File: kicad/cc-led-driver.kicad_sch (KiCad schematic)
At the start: 10 parts, among them Q3 PUMD9, U1 LMR33640ADDAR, U2 LM4040-2.5

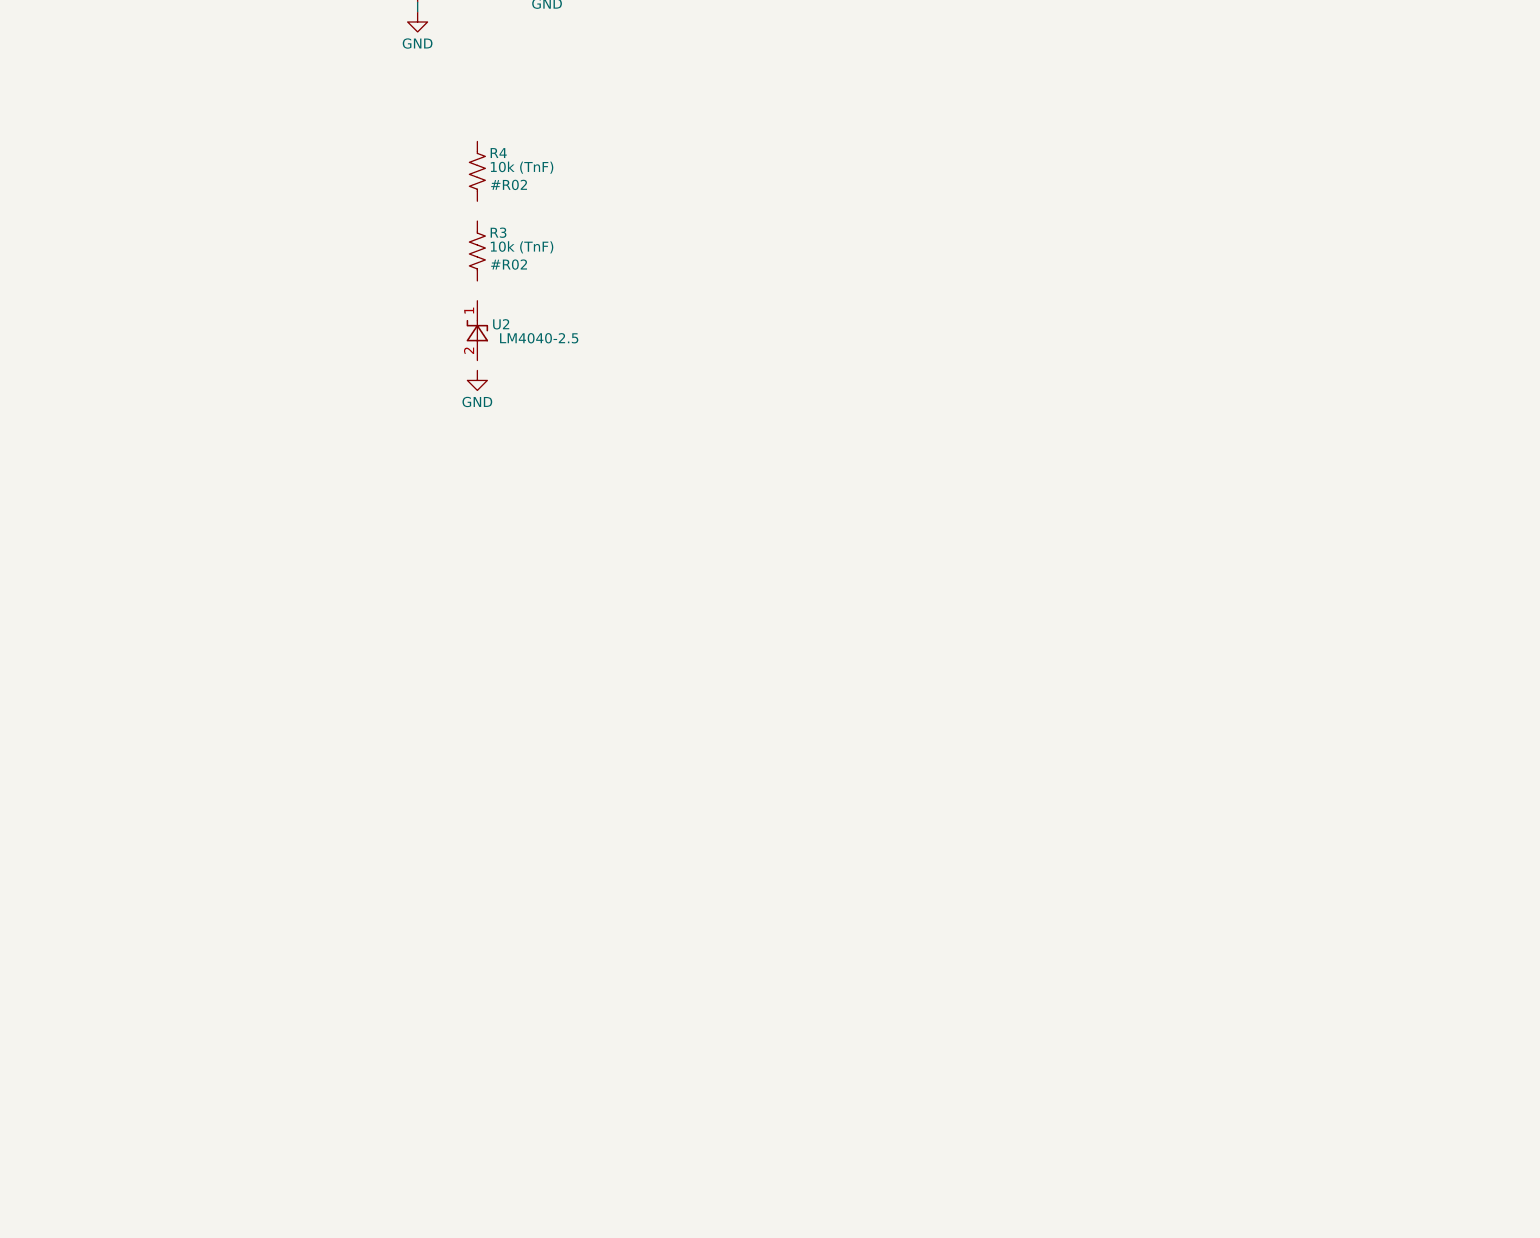
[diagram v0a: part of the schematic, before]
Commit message: gamma correction simulated
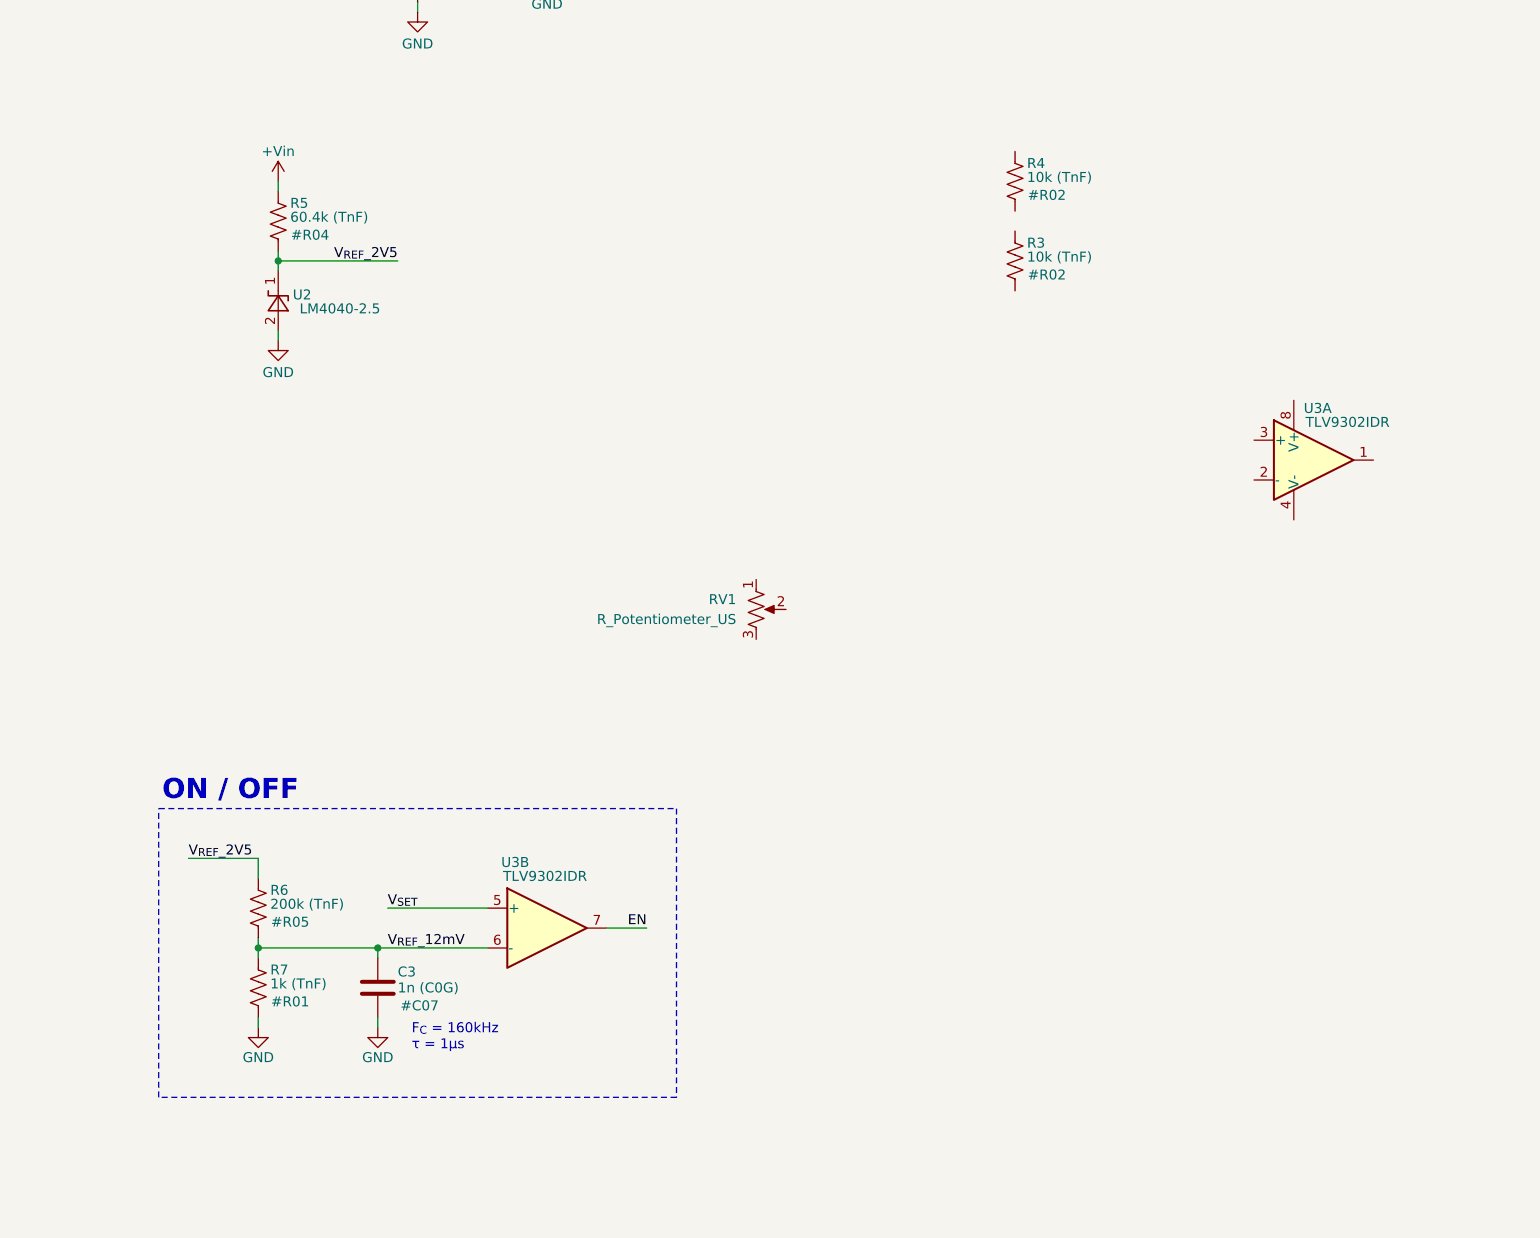
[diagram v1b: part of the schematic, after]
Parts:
- added C3: 1n (C0G), Capacitor_SMD:C_0603_1608Metric, symbol Device:C
- added R5: 60.4k (TnF), Resistor_SMD:R_0603_1608Metric, symbol Device:R_US
- added R6: 200k (TnF), Resistor_SMD:R_0603_1608Metric, symbol Device:R_US
- added R7: 1k (TnF), Resistor_SMD:R_0603_1608Metric, symbol Device:R_US
- added RV1: R_Potentiometer_US, symbol Device:R_Potentiometer_US
- added U3: TLV9302IDR, Package_SO:SOIC-8_3.9x4.9mm_P1.27mm, symbol Amplifier_Operational:TLV9302xD
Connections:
- net GND: now also U2.2 (A), C3.2, R7.2
- net V_{REF}_2V5: now reaches U2.1 (K)
- net V_{REF}_2V5: now also R5.2, R6.1
- new net +Vin: R5.1
- new net EN: U3.7
- new net V_{REF}_12mV: C3.1, R6.2, R7.1, U3.6 (-)
- new net V_{SET}: U3.5 (+)
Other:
- note added: "F_{C} = 160kHz τ = 1μs"
- note added: "ON / OFF"
- moved on the sheet: R3, R4, U2

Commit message: progress on schematic
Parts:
- added C10: DNP, Capacitor_SMD:C_0603_1608Metric, symbol Device:C
- added C11, C12, C13, C14, C15, C16, C17, C18, C19, C20: 10u (X7R), Capacitor_SMD:C_1210_3225Metric, symbol Device:C
- added C4, C5, C6, C9: 100n (X7R), Capacitor_SMD:C_0603_1608Metric, symbol Device:C
- added C7: 1n (C0G), Capacitor_SMD:C_0603_1608Metric, symbol Device:C
- added C8: 10n (C0G), Capacitor_SMD:C_0603_1608Metric, symbol Device:C
- added D1: BAV199Q-7-F, Package_TO_SOT_SMD:SOT-23, symbol Diode:BAV99
- added D6: BAT54-7-F, Package_TO_SOT_SMD:SOT-23, symbol Device:D_Schottky
- added Q1, Q2: MMBT3904-7-F, Package_TO_SOT_SMD:SOT-23, symbol Transistor_BJT:MMBT3904
- added R10, R20, R21, R25: 68k (TnF), Resistor_SMD:R_0603_1608Metric, symbol Device:R_US
- added R11: 28k (TnF), Resistor_SMD:R_0603_1608Metric, symbol Device:R_US
- added R12, R19, R24: 4.02k (TnF), Resistor_SMD:R_0603_1608Metric, symbol Device:R_US
- added R13, R15, R17, R18: 20k (TnF), Resistor_SMD:R_0603_1608Metric, symbol Device:R_US
- added R14, R8, R9: 100k (TnF), Resistor_SMD:R_0603_1608Metric, symbol Device:R_US
- added R16: 200k (TnF), Resistor_SMD:R_0603_1608Metric, symbol Device:R_US
- added R22: 1M (TnF), Resistor_SMD:R_0603_1608Metric, symbol Device:R_US
- added R23: 100R (TnF), Resistor_SMD:R_0603_1608Metric, symbol Device:R_US
- R5: CPN #R04 -> (none); now not fitted
- RV1: value R_Potentiometer_US -> 100k; footprint (none) -> Potentiometer_THT:Potentiometer_Bourns_PTV09A-1_Single_Vertical; Digikey (none) -> https://www.digikey.com/en/products/detail/bourns-inc/PTV09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
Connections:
- net +Vin: now also U3.8 (V+), C5.1, R13.1; no longer R5.1
- net EN: now also D1.1 (K)
- net FB: now also C10.2, Q2.3 (C), R20.1, R21.2
- net GND: now also R1.2, U3.4 (V-), C11.2, C12.2, C13.2, C14.2, C15.2, C16.2, C17.2, C18.2, C19.2, C20.2, C4.2, C5.2, C6.2, C9.2, R11.2, R16.2, R18.2, R20.2, R24.2, R9.2
- net V_{REF}_2V5: now also R10.1, R13.2, R8.1; no longer R5.2
- net V_{SET}: now also U3.3 (+), C4.1, Q1.2 (E), R9.1
- net at RV1.1: now also R10.2
- net at RV1.2: now also Q1.1 (B), R12.1
- net at RV1.3: now also R11.1, R12.2
- net V_{SENSE}: now reaches R4.1
- net V_{SENSE}: now also R1.1, C9.1
- net V_{OP-}: now reaches R4.2
- net V_{OP-}: now also U3.2 (-), C8.1, R22.1
- net BUCK_EN: now reaches U1.3 (EN)
- net BUCK_EN: now also C6.1, D1.2 (A), R16.1
- net V_{CFF}: now reaches U3.1
- net V_{CFF}: now also C8.2, R23.1
- net V_{OUT}: now reaches L1.2
- net V_{OUT}: now also C10.1, R21.1
- new net: C11.1, C12.1, C13.1, C14.1, C15.1, C16.1, C17.1, C18.1, C19.1, C20.1
- new net: Q1.3 (C), R8.2
- new net: Q2.1 (B), R25.1
- new net: Q2.2 (E), R24.1
- new net V_{CTRL}: R22.2, R23.2, R25.2
- no-connect marks 1 -> 2
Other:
- note added: "1.23V"
- note added: "7.1u / ea @ 13V"
- note added: "BRIGHTNESS CONTROL"
- note added: "CC SERVO"
- note added: "F_{SW} = 400kHz"
- note added: "G ≈ 100 (40dB) F_{-3dB} ≈ 16Hz Φ_{M} ≈ 64°"
- note added: "T_{ON} = 2μs T_{OFF} = 160ms"
- note added: "VREF"
- note added: "[2V, 19V]"
- moved on the sheet: C1, C2, C3, L1, R1, R3, R4, R6, R7, RV1, U1, U2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

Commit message: sync
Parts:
- added FB1: MH2029-300T, Inductor_SMD:L_0805_2012Metric, symbol Device:FerriteBead
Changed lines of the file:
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@@
+	)
+	(symbol
+		(lib_id "Device:FerriteBead")
+		(at 41.91 43.18 90)
+		(unit 1)
+		(exclude_from_sim no)
+		(in_bom yes)
+		(on_board yes)
+		(dnp no)
+		(property "Reference" "FB1"
+			(at 34.544 37.338 90)
+			(effects
+				(font
+					(size 1.27 1.27)
+				)
+				(justify right)
+			)
+		)
+		(property "Value" "MH2029-300T"
+			(at 34.544 39.1669 90)
+			(effects
+				(font
+					(size 1.27 1.27)
+				)
+				(justify right)
+			)
+		)
+		(property "Footprint" "Inductor_SMD:L_0805_2012Metric"
+			(at 41.91 44.958 90)
+			(effects
+				(font
+					(size 1.27 1.27)
+				)
+				(hide yes)
+			)
+		)
+		(property "Datasheet" "https://www.bourns.com/docs/Product-Datasheets/MH2029-T.pdf"
+			(at 41.91 43.18 0)
+			(effects
+				(font
+					(size 1.27 1.27)
+				)
+				(hide yes)
+			)
+		)
+		(property "Description" "30 Ohms @ 100 MHz 1 Power, Signal Line Ferrite Bead 0805 (2012 Metric) 8.5A 4mOhm"
+			(at 41.91 43.18 0)
+			(effects
+				(font
+					(size 1.27 1.27)
+				)
+				(hide yes)
+			)
+		)
+		(property "Digikey" "https://www.digikey.com/en/products/detail/bourns-inc/MH2029-300T/21556186"
+			(at 41.91 43.18 0)
+			(effects
+				(font
+					(size 1.27 1.27)
+				)
+				(hide yes)
+			)
+		)
+		(pin "1"
+		)
+		(pin "2"
+		)
+		(instances
+			(project ""
+				(path "/6c6605c9-2b9a-4fed-8d75-2a02c2ded1b0"
+					(reference "FB1")
+					(unit 1)
+				)
+			)
+		)
 	)
 	(symbol

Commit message: completed schematic and ordered gerbers
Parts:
- removed D6: BAT54-7-F, Package_TO_SOT_SMD:SOT-23, symbol Device:D_Schottky
- removed Q3: PUMD9, Package_TO_SOT_SMD:SOT-363_SC-70-6, symbol Transistor_BJT:PUMX1
- removed R14: 100k (TnF), Resistor_SMD:R_0603_1608Metric, symbol Device:R_US
- removed R15, R17, R18: 20k (TnF), Resistor_SMD:R_0603_1608Metric, symbol Device:R_US
- removed R19: 4.02k (TnF), Resistor_SMD:R_0603_1608Metric, symbol Device:R_US
- removed R5: 60.4k (TnF), Resistor_SMD:R_0603_1608Metric, symbol Device:R_US
- added C1, C5: 100n (X7R), Capacitor_SMD:C_0603_1608Metric, symbol Device:C
- added C3, C4: 10u (X7R), Capacitor_SMD:C_1210_3225Metric, symbol Device:C
- added F1: 3A, Fuse:Fuse_1206_3216Metric, symbol Device:Fuse
- added H1, H2, H3, H4: M3, MountingHole:MountingHole_2.2mm_M2_DIN965_Pad, symbol Mechanical:MountingHole_Pad
- added J1: VSUP, 20AWG:20AWG, symbol Connector_Generic:Conn_01x01
- added J2: GND, 20AWG:20AWG, symbol Connector_Generic:Conn_01x01
- added J3: Vout, 20AWG:20AWG, symbol Connector_Generic:Conn_01x01
- added J4: Vsense, 20AWG:20AWG, symbol Connector_Generic:Conn_01x01
- added R9: 50m (TkF), Resistor_SMD:R_0603_1608Metric, symbol Device:R_US
- C7: value 1n (C0G) -> 100n (X7R); CPN #C07 -> #C02; Digikey https://www.digikey.com/en/products/detail/murata-electroni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 -> https://www.digikey.com/en/products/detail/samsung-electro-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
- R3: value 10k (TnF) -> 1 (TnF); CPN #R02 -> #R11; Digikey https://www.digikey.com/en/products/detail/vishay-beyschlag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 -> https://www.digikey.com/en/products/detail/vishay/MCT06030C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
- renumbered C2 to C10, C8 to C11, C5 to C12, C10 to C13, C11 to C14, C16 to C15, C12 to C16, C13 to C18, C18 to C19, C3 to C2, C14 to C20, C19 to C21, C15 to C22, C20 to C23, C9 to C24, C4 to C6, C6 to C8, C1 to C9, R2 to R1, R8 to R10, R9 to R11, R16 to R12, R4 to R13, R21 to R14, R20 to R15, R22 to R16, R24 to R17, R23 to R18, R25 to R19, R13 to R2, R1 to R20, R6 to R4, R7 to R5, R10 to R6, R11 to R7, R12 to R8, U2 to U1, U3 to U2, U1 to U3
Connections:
- net +Vin: now also C7.1, FB1.2, U3.2 (VIN), C5.1, R9.1
- net GND: now also C7.2, C1.2, C3.2, C4.2, C5.2, H1.1, H2.1, H3.1, H4.1, J2.1 (Pin_1)
- net V_{OUT}: now also C14.1, C15.1, C16.1, C17.1, C18.1, C19.1, C20.1, C21.1, C22.1, C23.1, J3.1 (Pin_1)
- net V_{SENSE}: now also J4.1 (Pin_1)
- net V_{SUP}: now reaches R3.1
- net V_{SUP}: now also F1.1, J1.1 (Pin_1)
- net at R3.2: now also C1.1
- net at FB1.1: now also F1.2
- new net: C3.1, C4.1, R9.2
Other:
- note added: "BUCK CONVERTER"
- note added: "C WITH FILTER"
- note added: "EXTRA / DNP"
- note added: "F_{-3dB} ≈ 253kHz DC_{R} ≈ 54mΩ"
- note added: "Gamma Correction and V_{REF} Divsion"
- note added: "IN"
- note added: "INPUT FILTER"
- note added: "OUT"
- note added: "SHUNT"
- note added: "[0A, 3A]"
- moved on the sheet: C10, C11, C12, C13, C14, C15, C16, C17, C18, C19, C2, C20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
